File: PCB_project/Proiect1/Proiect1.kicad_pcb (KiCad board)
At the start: 2 copper layers, 40 x 40 mm, 36 parts, among them J1 Vout, J2 GND, J3 +25V, J4 GND, Q1 BC846, Q10 BC846, Q11 BC846, Q12 BC856, Q13 BC856, Q2 BC856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

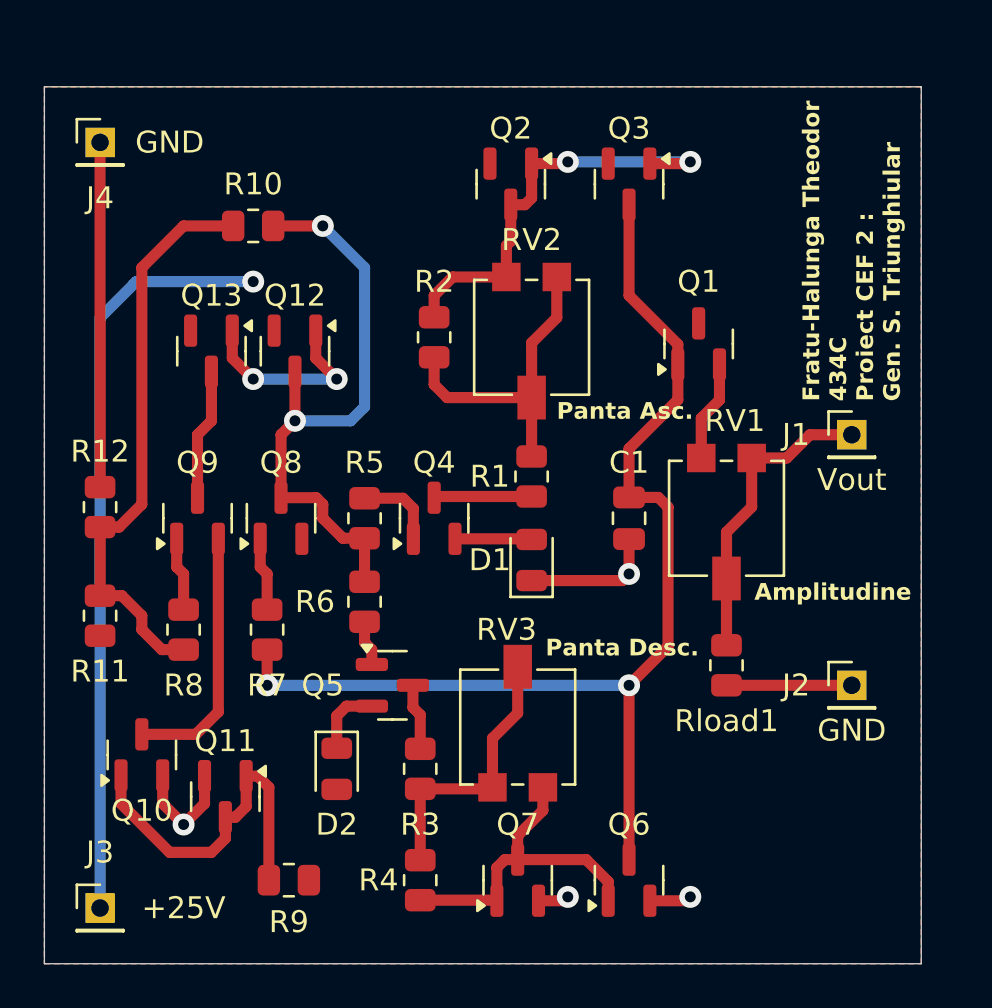
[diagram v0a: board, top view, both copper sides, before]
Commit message: Updated PCB to conform with Manufacturing Requirements
Changed trace widths form 20 mils to 16 mils. Changed via sizes from 0.5mm/1mm to 0.4mm/1mm. Changed edge clearance from 0.5mm to 1mm. Changed trace clearance from 5? mils to 14 mils. Added 3 fiducials of size 1mm/2mm.

Still need to see what is up with that MECHANIC layer. Need to generate a mechanical drawing for the board edge, a drill drawing, a drill table and a drill legend as well as a layer stackup (technically KiCad already did this for me automatically but I don't know if this needs to be included in this MECHANIC layer or not)
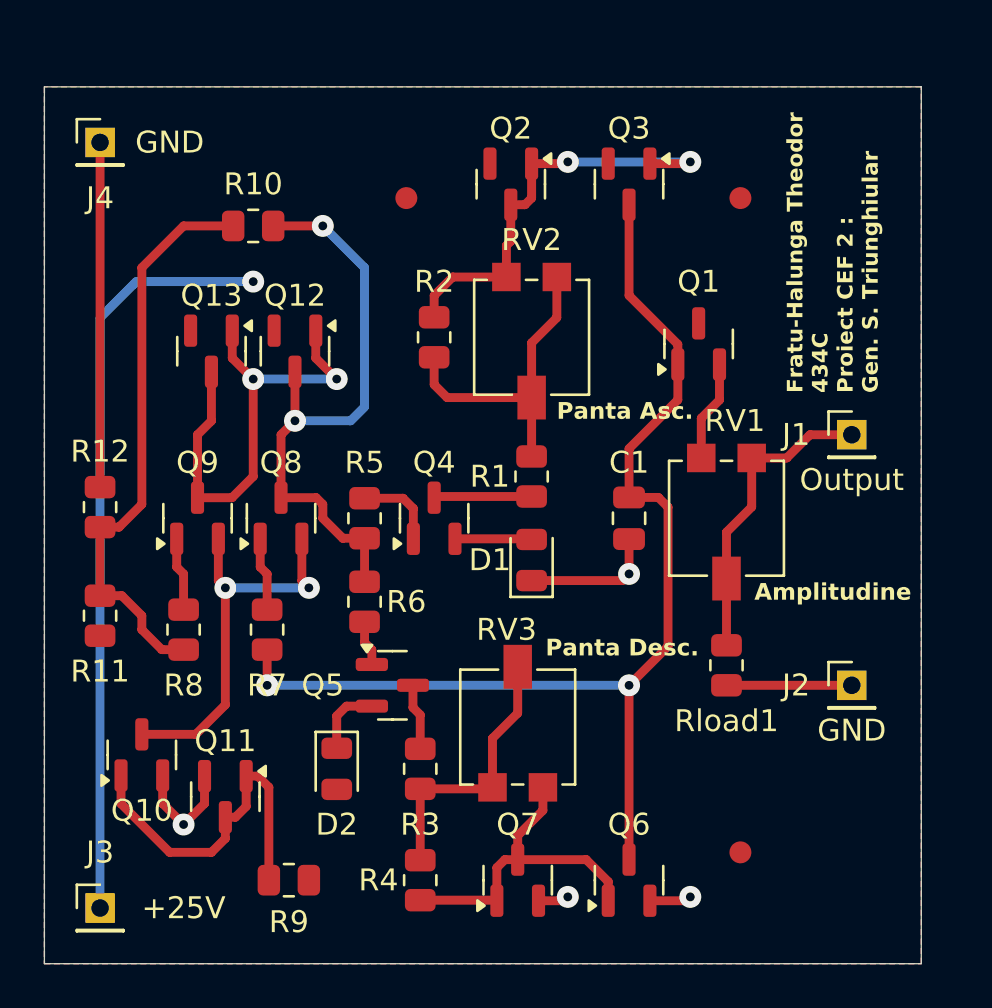
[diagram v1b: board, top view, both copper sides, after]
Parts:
- added FID1: Fiducial, Fiducial:Fiducial_1mm_Mask2mm, F.Cu at (141.5, 80.1)
- added FID2: Fiducial, Fiducial:Fiducial_1mm_Mask2mm, F.Cu at (156.8, 80.1)
- added FID3: Fiducial, Fiducial:Fiducial_1mm_Mask2mm, F.Cu at (156.8, 109.9)
- J1: value Vout -> Output
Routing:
- net Net-(Q12-B): track 15.0 -> 22.4 mm
- net Net-(Q10-C): track 11.8 -> 18.3 mm, vias 0 -> 2

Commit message: Changed jumpers from THT to SMD
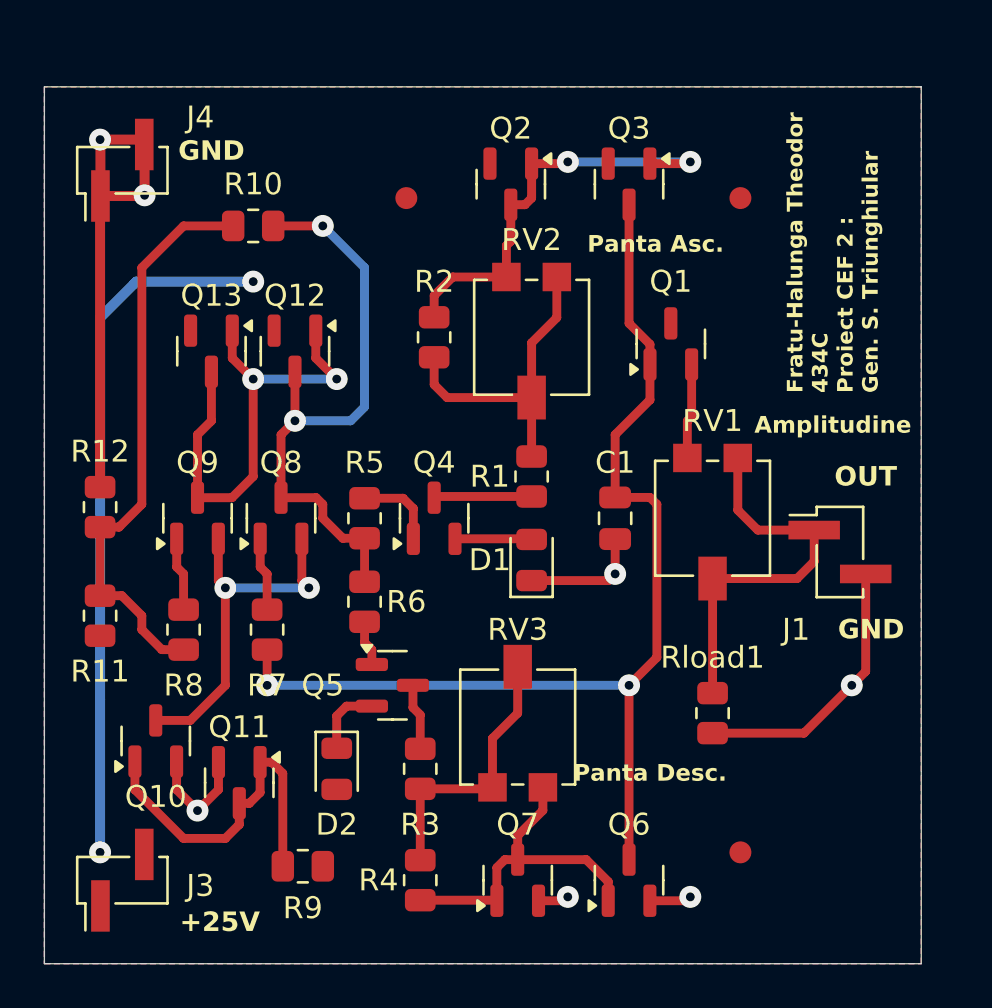
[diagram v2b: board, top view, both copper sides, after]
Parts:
- removed J2: GND, Connector_PinHeader_2.00mm:PinHeader_1x01_P2.00mm_Vertical
- J1: value Output -> OUT; footprint Connector_PinHeader_2.00mm:PinHeader_1x01_P2.00mm_Vertical -> Connector_PinHeader_2.00mm:PinHeader_1x02_P2.00mm_Vertical_SMD_Pin1Left
- J3, J4: footprint Connector_PinHeader_2.00mm:PinHeader_1x01_P2.00mm_Vertical -> Connector_PinHeader_2.00mm:PinHeader_1x02_P2.00mm_Vertical_SMD_Pin1Left
- moved J1 5.38 mm to (161.3, 96.2)
- moved Rload1 2.27 mm to (155.5, 103.6)
- moved J4 1.63 mm to (128.6, 78.8), turned to 90 degrees
- moved J3 1.63 mm to (128.6, 111.2), turned to 90 degrees
- moved Q1 1.27 mm to (153.6, 86.7)
- moved Q10 0.90 mm to (130.1, 104.8)
- moved Q11 0.90 mm to (133.9, 106.7)
- moved R9 0.90 mm to (136.8, 110.6)
- moved RV1 0.64 mm to (155.5, 94.7)
- moved C1 0.63 mm to (151.0, 94.7)
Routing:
- net GND: track 36.2 -> 49.0 mm, vias 4 -> 7
- net Net-(J1-Pin_1): track 14.0 -> 17.9 mm
- net +25V: track 34.6 -> 32.1 mm, vias 1 -> 2
- net Net-(Q10-C): track 18.3 -> 16.8 mm
- net Net-(Q1-B): track 52.1 -> 51.3 mm
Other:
- board text added: "GND"
